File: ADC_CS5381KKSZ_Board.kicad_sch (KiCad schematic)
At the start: 115 parts, among them IC1 OpAmp_NE5532D, J1 Mode_Selection_Jumpers, J10 JST_XH_2.54_Plug_12V+, J11 JST_XH_2.54_Plug_12V-, J12 I2S_Headers, J13 MCLK_DIV_Jumper, J14 JST_XH_2.54_Plug_5V+, J15 USB_B_Micro, J16 USB_D_Jumper, J17 MCLK_Jumper, J2 JST_XH_2.54_Plug_3V3+, J3 3V3_Power_Selector_Jumper, J4 3V_Selection_Header, J5 I/O_Headers, J6 I2S_OR_LJ_OUT, J7 I2S_OR_LJ_OUT, J8 HP_FILTER_EN, J9 I/O_Headers, Q1 MOSFET_SI2333DDS-T1-BE3, Q2 MOSFET_SI2333DDS-T1-BE3, Q3 MOSFET_SI2343DS-T1-BE3, Q4 MOSFET_SI2343DS-T1-BE3, U1 CS5381

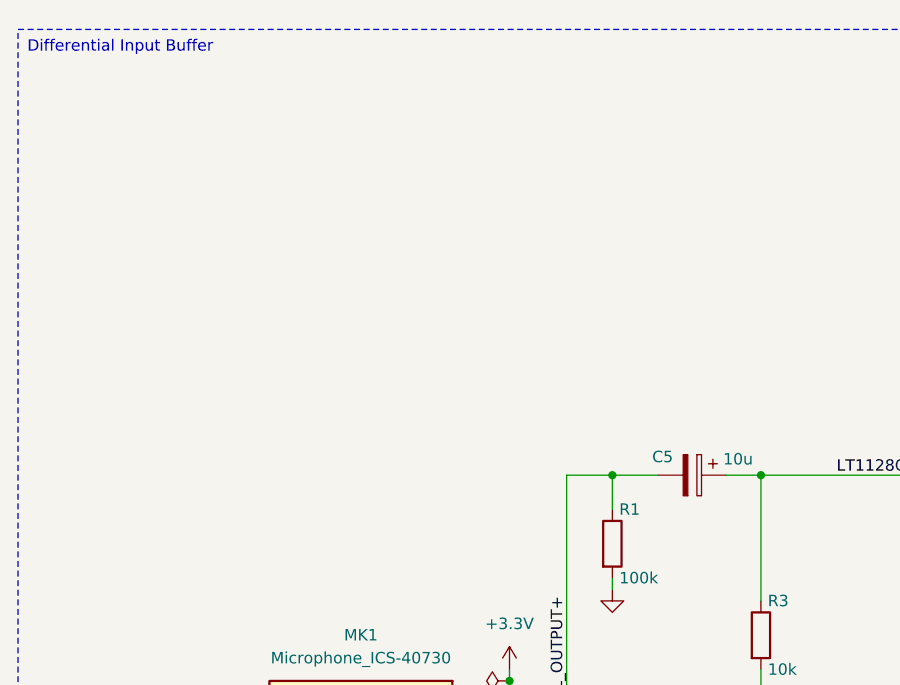
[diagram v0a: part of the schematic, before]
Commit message: Added ADC Driver
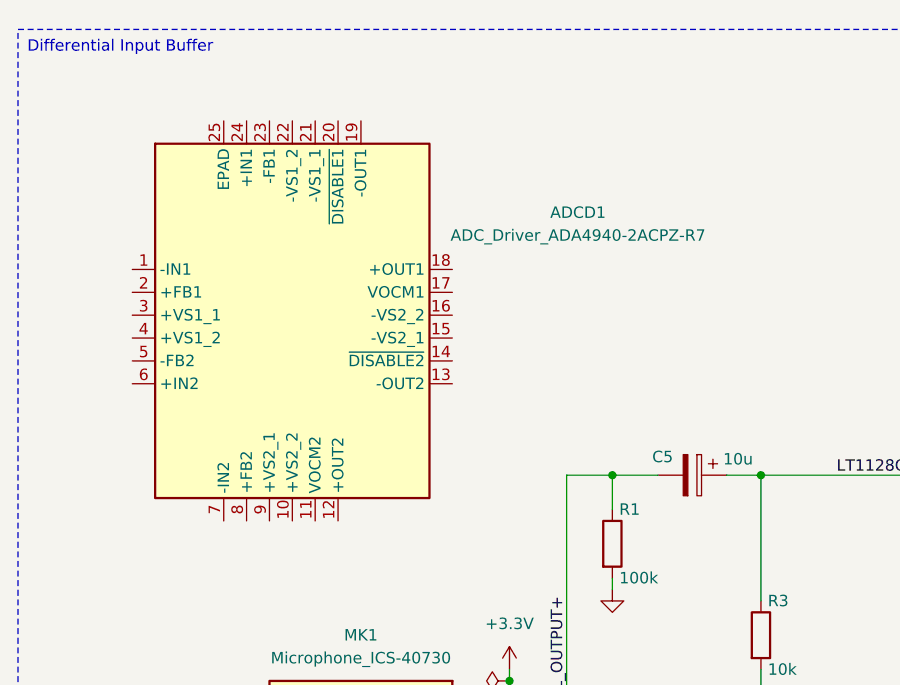
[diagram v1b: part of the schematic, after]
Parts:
- added ADCD1: ADC_Driver_ADA4940-2ACPZ-R7, Personal_Project:ADC_Driver_ADA4940-2ACPZ-R7_QFN50P400X400X80-25N-D, symbol Personal_Projects:ADC_Driver_ADA4940-2ACPZ-R7
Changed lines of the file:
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@@
+	)
+	(symbol
+		(lib_id "Personal_Projects:ADC_Driver_ADA4940-2ACPZ-R7")
+		(at 33.02 48.26 0)
+		(unit 1)
+		(exclude_from_sim no)
+		(in_bom yes)
+		(on_board yes)
+		(dnp no)
+		(fields_autoplaced yes)
+		(property "Reference" "ADCD1"
+			(at 85.09 41.9414 0)
+			(effects
+				(font
+					(size 1.27 1.27)
+				)
+			)
+		)
+		(property "Value" "ADC_Driver_ADA4940-2ACPZ-R7"
+			(at 85.09 44.4814 0)
+			(effects
+				(font
+					(size 1.27 1.27)
+				)
+			)
+		)
+		(property "Footprint" "Personal_Project:ADC_Driver_ADA4940-2ACPZ-R7_QFN50P400X400X80-25N-D"
+			(at 69.85 127.94 0)
+			(effects
+				(font
+					(size 1.27 1.27)
+				)
+				(justify left top)
+				(hide yes)
+			)
+		)
+		(property "Datasheet" "https://www.analog.com/ADA4940-2/datasheet"
+			(at 69.85 227.94 0)
+			(effects
+				(font
+					(size 1.27 1.27)
+				)
+				(justify left top)
+				(hide yes)
+			)
+		)
+		(property "Description" "Small signal bandwidth: 260 MHz Ultralow power 1.25mA Extremely low harmonic distortion 122 dB THD at 50 kHz 96 dB THD at 1 MHz Low input voltage noise: 3.9 nV/Hz 0.35 mV maximum offset voltage Balanced outputs Settling time to 0.1%: 34 ns Rail-to-rail output: VS + 0.1 V to +VS  0.1 V Adjustable output common-mode voltage Flexible power supplies: 3 V to 7 V (LFCSP) Disable pin to reduce power consumption ADA4940-1 is available in LFCSP and SOIC packages"
+			(at 33.274 92.202 0)
+			(effects
+				(font
+					(size 1.27 1.27)
+				)
+				(hide yes)
+			)
+		)
+		(property "Height" "0.8"
+			(at 69.85 427.94 0)
+			(effects
+				(font
+					(size 1.27 1.27)
+				)
+				(justify left top)
+				(hide yes)
+			)
+		)
+		(property "Mouser Part Number" "584-ADA4940-2ACPZ-R7"
+			(at 69.85 527.94 0)
+			(effects
+				(font
+					(size 1.27 1.27)
+				)
+				(justify left top)
+				(hide yes)
+			)
+		)
+		(property "Mouser Price/Stock" "https://www.mouser.co.uk/ProductDetail/Analog-Devices/ADA4940-2ACPZ-R7?qs=BpaRKvA4VqHtamCKy8fS8Q%3D%3D"
+			(at 69.85 627.94 0)
+			(effects
+				(font
+					(size 1.27 1.27)
+				)
+				(justify left top)
+				(hide yes)
+			)
+		)
+		(property "Manufacturer_Name" "Analog Devices"
+			(at 69.85 727.94 0)
+			(effects
+				(font
+					(size 1.27 1.27)
+				)
+				(justify left top)
+				(hide yes)
+			)
+		)
+		(property "Manufacturer_Part_Number" "ADA4940-2ACPZ-R7"
+			(at 69.85 827.94 0)
+			(effects
+				(font
+					(size 1.27 1.27)
+				)
+				(justify left top)
+				(hide yes)
+			)
+		)
+		(pin "6"
+		)
+		(pin "7"
+		)
+		(pin "4"
+		)
+		(pin "5"
+		)
+		(pin "25"
+		)
+		(pin "3"
+		)
+		(pin "18"
+		)
+		(pin "19"
+		)
+		(pin "23"
+		)
+		(pin "24"
+		)
+		(pin "21"
+		)
+		(pin "22"
+		)
+		(pin "16"
+		)
+		(pin "17"
+		)
+		(pin "8"
+		)
+		(pin "9"
+		)
+		(pin "12"
+		)
+		(pin "11"
+		)
+		(pin "2"
+		)
+		(pin "20"
+		)
+		(pin "10"
+		)
+		(pin "15"
+		)
+		(pin "14"
+		)
+		(pin "1"
+		)
+		(pin "13"
+		)
+		(instances
+			(project ""
+				(path "/532b720a-d345-4e8b-bed0-e606731588e9"
+					(reference "ADCD1")
+					(unit 1)
+				)
+			)
+		)
 	)
 	(symbol

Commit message: Update ADC_CS5381KKSZ_Board.kicad_sch
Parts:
- removed C14, C15, C5, C6: 10u, Capacitor_SMD:C_0805_2012Metric, symbol Device:C_Polarized
- removed C16, C19: 470p_C0G, Capacitor_SMD:C_0805_2012Metric, symbol Device:C
- removed C17, C18, C20, C21: 100n_X7R, Capacitor_SMD:C_0805_2012Metric, symbol Device:C
- removed C22: 2700p_C0G, Capacitor_SMD:C_0805_2012Metric, symbol Device:C
- removed OA1, OA2, OA3, OA4: LT1128CS8, Personal_Project:OpAmp_LT1128CS8_SOIC127P599X175-8N, symbol Personal_Projects:OpAmp_LT1128CS8
- removed R10, R9: 100k, Resistor_SMD:R_0805_2012Metric, symbol Device:R
- removed R11, R12, R4: 10k, Resistor_SMD:R_0805_2012Metric, symbol Device:R
- removed R13, R14, R6, R7: 634, Resistor_SMD:R_0805_2012Metric, symbol Device:R
- removed R15, R16, R5, R8: 91, Resistor_SMD:R_0805_2012Metric, symbol Device:R
- added C14, C5, C6: 100n, Capacitor_SMD:C_0805_2012Metric, symbol Device:C
- C10: value 470p_C0G -> 100n
- C11, C7: value 100n_X7R -> 10u
- C12, C8: value 100n_X7R -> 100n
- C13: value 2700p_C0G -> 10u
- C9: value 470p_C0G -> 10u
- R3: value 10k -> 100k
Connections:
- net L1_IN- is gone; now on net -VS2: C9.1
- net L2_IN- is gone; now on net -VS2: C10.1
- net LT1128CS8_L1_IN+ is gone; now on an unnamed net: R3.1
- net LT1128CS8_L1_OUT is gone; now on net GND: C9.2
- net LT1128CS8_L2_OUT is gone; now on net GND: C10.2
- net +12V: no longer C11.1, C7.1
- net -12V: no longer C12.1, C8.1
- net AINL+: no longer C13.2
- net AINL-: no longer C13.1
- net GND: now also ADCD1.25 (EPAD), C13.2, R2.1, C14.2, C5.2, C6.2; no longer R1.2, R2.2
- net MIC_L_OUTPUT+: now also R2.2
- net MIC_L_OUTPUT-: no longer R2.1
- net VCOM_B_LEFT: now also ADCD1.17 (VOCM1), C6.1; no longer R3.2
- net VCOM_B_RIGHT: now also ADCD1.11 (VOCM2), C5.1
- net +VS2: now reaches ADCD1.10 (+VS2_2)
- net +VS2: now also ADCD1.9 (+VS2_1), C12.1, C13.1
- net -OUT2: now reaches ADCD1.13 (-OUT2)
- net ~{DISABLE2}_ADA4940: now reaches ADCD1.14 (~{DISABLE2})
- net -VS2: now reaches ADCD1.15 (-VS2_1)
- net -VS2: now also ADCD1.16 (-VS2_2)
- net +OUT1: now reaches ADCD1.18 (+OUT1)
- net ~{DISABLE1}_ADA4940: now reaches ADCD1.20 (~{DISABLE1})
- net -VS1: now reaches ADCD1.21 (-VS1_1)
- net -VS1: now also ADCD1.22 (-VS1_2), C7.1, C8.1
- net at ADCD1.23 (-FB1): now also R3.2
- net at ADCD1.24 (+IN1): now also R1.2
- net +VS1: now reaches ADCD1.3 (+VS1_1)
- net +VS1: now also ADCD1.4 (+VS1_2), C11.1, C14.1
- no-connect marks 18 -> 6
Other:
- note added: "- DISABLE is asserted by applying a low - The DISABLE pin features an internal pull-up network that enables the amplifier for normal operation. The ADA4940-1/ ADA4940-2 DISABLE pin can be left floating (that is, no external connection is required) and does not require an external pull-up resistor to ensure normal on operation"
- note added: "It is also possible to connect the VOCM input to a common-mode level (CML) output of an ADC. However, care must be taken to ensure that the output has sufficient drive capability. The input impedance of the VOCM pin is approximately 250 kΩ."
- note added: "Output Impedance OUTPUT+ is 180 Ohms OUTPUT- is 250 Ohms"
- note added: "Resistor added to match input impedance to 50Ohms"
- moved on the sheet: ADCD1, MK1, MK3

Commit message: Update ADC_CS5381KKSZ_Board.kicad_sch
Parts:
- added C15, C16: 10u, Capacitor_SMD:C_0805_2012Metric, symbol Device:C
- added C17, C18: 100n, Capacitor_SMD:C_0805_2012Metric, symbol Device:C
- added R4, R5: 100k, Resistor_SMD:R_0805_2012Metric, symbol Device:R
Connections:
- net +3.3V: now also C17.1, C18.1
- net AINL+: now also R4.2, R5.1
- net GND: now also C17.2, C18.2, R4.1
- net MIC_L_OUTPUT+: now also C15.1; no longer R1.1, R2.2
- net MIC_L_OUTPUT-: now also C16.1
- net -OUT1: now reaches ADCD1.19 (-OUT1)
- net -OUT1: now also R5.2
- new net: C15.2, R1.1, R2.2
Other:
- note added: "Maximum Output Voltage Single-Ended, 123 dB SPL input is 0.40V rms This is Vpp≈1.13 V."
- note added: "Output DC Offset OUTPUT+ is 0.72V OUTPUT- is 0.66V"
- note added: "The two resistors set the open loop gain G = 2.5 Per leg"
- moved on the sheet: R1, R2

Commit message: Update ADC_CS5381KKSZ_Board.kicad_sch
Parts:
- removed C32: 4u7, Capacitor_SMD:C_0805_2012Metric, symbol Device:C
- removed C39, C41: 47u, Capacitor_SMD:C_0805_2012Metric, symbol Device:C_Polarized
- removed C40, C42: 10n_X7R, Capacitor_SMD:C_0805_2012Metric, symbol Device:C
- removed D1: BZX84C4V3LT1G, Package_TO_SOT_SMD:SOT-23, symbol Diode:BZX84Cxx
- removed D4, D5: BZX84C13LT1G, Package_TO_SOT_SMD:SOT-23, symbol Diode:BZX84Cxx
- removed J10: JST_XH_2.54_Plug_12V+, Personal_Project:Connector_Power2pin_SHDRRA2W80P0X250_1X2_740X1150X610P, symbol Personal_Projects:Connector_Power2pin_JST_XH_2.54_Plug
- removed J11: JST_XH_2.54_Plug_12V-, Personal_Project:Connector_Power2pin_SHDRRA2W80P0X250_1X2_740X1150X610P, symbol Personal_Projects:Connector_Power2pin_JST_XH_2.54_Plug
- removed J12: I2S_Headers, Connector_PinHeader_2.54mm:PinHeader_2x03_P2.54mm_Horizontal, symbol Connector_Generic:Conn_02x03_Odd_Even
- removed J2: JST_XH_2.54_Plug_3V3+, Personal_Project:Connector_Power2pin_SHDRRA2W80P0X250_1X2_740X1150X610P, symbol Personal_Projects:Connector_Power2pin_JST_XH_2.54_Plug
- removed J3: 3V3_Power_Selector_Jumper, Connector_PinHeader_2.54mm:PinHeader_2x03_P2.54mm_Vertical, symbol Connector_Generic:Conn_02x03_Odd_Even
- removed J4: 3V_Selection_Header, Connector_PinHeader_2.54mm:PinHeader_1x03_P2.54mm_Vertical, symbol Connector_Generic:Conn_01x03
- removed J9: I/O_Headers, Connector_PinHeader_2.54mm:PinHeader_2x05_P2.54mm_Horizontal, symbol Connector_Generic:Conn_02x05_Odd_Even
- removed Q1: MOSFET_SI2333DDS-T1-BE3, Personal_Project:MOSFET_ SI2333DDS_SOT_DS-T1-BE3_VIS, symbol Personal_Projects:MOSFET_SI2333DDS-T1-BE3
- removed Q3, Q4: MOSFET_SI2343DS-T1-BE3, Personal_Project:MOSFET_ SI2333DDS_SOT_DS-T1-BE3_VIS, symbol Personal_Projects:MOSFET_SI2333DDS-T1-BE3
- removed R18, R19, R2, R26: 100k, Resistor_SMD:R_0805_2012Metric, symbol Device:R
- removed Z1, Z3, Z4: Diode_BZX84C6V2-7-F, Personal_Project:Diode_BZX84C6V2_SOT96P240X110-3N, symbol Personal_Projects:Diode_BZX84C6V2-7-F
- added C19, C20: 10u, Capacitor_SMD:C_0805_2012Metric, symbol Device:C
- added C21, C22: 2n7, Capacitor_SMD:C_0805_2012Metric, symbol Device:C
- added FPC1: I2S_FPC_Header, Personal_Project:FPC_SAMTEC_ZF5S-20-01-T-WT, symbol Personal_Projects:FPC_ZF5S-20-01-T-WT
- added J2: I2S_OR_LJ_OUT, Connector_PinHeader_2.54mm:PinHeader_1x03_P2.54mm_Vertical, symbol Connector_Generic:Conn_01x03
- added J3: I/O_Headers_1, symbol Connector_Generic:Conn_02x06_Odd_Even
- added R10, R12, R7: 200R, Resistor_SMD:R_0805_2012Metric, symbol Device:R
- added R11: 500R, Resistor_SMD:R_0805_2012Metric, symbol Device:R
- added R13, R14: 22R, Resistor_SMD:R_0805_2012Metric, symbol Device:R
- added R6, R9: 500k, Resistor_SMD:R_0805_2012Metric, symbol Device:R
- J5: value I/O_Headers -> I/O_Headers_2
- R1: value 100k -> 200R
- R17: value 22R1 -> 22R
- R3: value 100k -> 500R
- R4, R5: value 100k -> 22R
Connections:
- net +12V is gone; now on net +5VA: C1.1
- net +VS2 is gone; now on net +VS1: ADCD1.10 (+VS2_2), ADCD1.9 (+VS2_1), C12.1, C13.1
- net -12V is gone; now on net GND: C2.2
- net -VS2 is gone; now on net -VS1: ADCD1.15 (-VS2_1), ADCD1.16 (-VS2_2), C10.1, C9.1
- net LDO_IN is gone; now on net +5VA: C30.1, LDO1.1 (IN), LDO1.3 (EN)
- net LD_OUT_3V3 is gone; now on net +3.3V: C31.1, LDO1.5 (OUT)
- net +3.3V: no longer S1.2
- net +OUT1: now also R4.1
- net -OUT1: now also R5.1; no longer R5.2
- net -OUT2: now also R13.1
- net AINL+: now also C21.2; no longer R5.1
- net AINL-: now also R5.2, C21.1
- net AINR+: now also C22.2, R14.2
- net AINR-: now also C22.1, R13.2
- net EXT_POWER_5V+_PP: now also J2.3 (Pin_3); no longer C33.1, C34.1, D3.3 (K), FB1.1
- net GND: now also FPC1.01, FPC1.03, FPC1.04, FPC1.05, FPC1.06, FPC1.07, FPC1.08, FPC1.09, FPC1.10, FPC1.12, FPC1.13, FPC1.14, FPC1.15, FPC1.16, FPC1.18, FPC1.19, FPC1.20, J3.10 (Pin_10), J3.12 (Pin_12), J3.2 (Pin_2), J3.4 (Pin_4), J3.6 (Pin_6), J3.8 (Pin_8); no longer R4.1
- net LRCK: now also FPC1.11
- net M0: now also J3.1 (Pin_1)
- net M1: now also J3.3 (Pin_3)
- net MCLK_EXT: now also J3.7 (Pin_7)
- net MDIV: now also J3.5 (Pin_5)
- net MIC_R_OUTPUT+: now also C19.1
- net MIC_R_OUTPUT-: now also C20.1
- net SCLK: now also FPC1.17
- net SDOUT: now also FPC1.02
- net ~{DISABLE1}_ADA4940: now also J3.9 (Pin_9)
- net ~{DISABLE2}_ADA4940: now also J3.11 (Pin_11)
- net at ADCD1.1 (-IN1): now also R6.2, R7.2
- net at ADCD1.12 (+OUT2): now also R14.1
- net at ADCD1.2 (+FB1): now also R6.1
- net at ADCD1.5 (-FB2): now also R9.2
- net at ADCD1.6 (+IN2): now also R10.2, R9.1
- net at ADCD1.7 (-IN2): now also R11.1, R12.2
- net at ADCD1.8 (+FB2): now also R11.2
- net at C16.2: now also R7.1
- net POWER_3V3: no longer names the net of S1.1
- net POWER_3V3: now also C33.1, C34.1, D3.3 (K), FB1.1
- net VBUS_5V renamed USB_VBUS_5V
- net USB_VBUS_5V: now also J2.1 (Pin_1)
- new net: J2.2 (Pin_2), S1.2
- new net: C20.2, R12.1
- new net: C19.2, R10.1
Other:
- note added: "Amplify Microphone output: 0.4Vrms (0.565685424949Vpeak) 0.565685424949Vpeak*2 = 1.1313708499Vpp to 2.82Vpp with 2.5V DC 2.82V/1.1313708499Vpp = 2.49255140368 Gain"
- note added: "Disable Pins Active LOW"
- note added: "Frequency Response from 20 Hz to 20 kHz"
- note added: "Fullscale Input Level = (Ain+)-(Ain-) = 5.64 Vpp Ain+ is between 3.91 and 1.09 V (Each leg swinging 2.82V) Ain- is between 3.91 and 1.09 V Both oscillate around 2.5V (Common mode level) The DC bias (Common mode level) is sett using VQ or VCOM (one pin) VQ or VCOM nominal voltage is 2.5V Filt+ Nominal Voltage 5V (Positive voltage reference output)"
- note added: "Input voltage range: 5V (Exact)"
- note added: "Output Impedance OUTPUT+ is 180 Ohms OUTPUT- is 250 Ohms Differential is 430 Ohms"
- note added: "Pin 2 connects to one or three"
- note added: "RST - Enters low power modde when LOW"
- note added: "length-matched"
- note removed: "Input voltage range: 1.45V to 5.5V"
- note removed: "Output Impedance OUTPUT+ is 180 Ohms OUTPUT- is 250 Ohms"
- note removed: "Resistor added to match input impedance to 50Ohms"
- moved on the sheet: ADCD1, C10, C11, C12, C13, C14, C15, C16, C17, C18, C23, C24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
